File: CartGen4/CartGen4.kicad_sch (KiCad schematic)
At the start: 0 parts

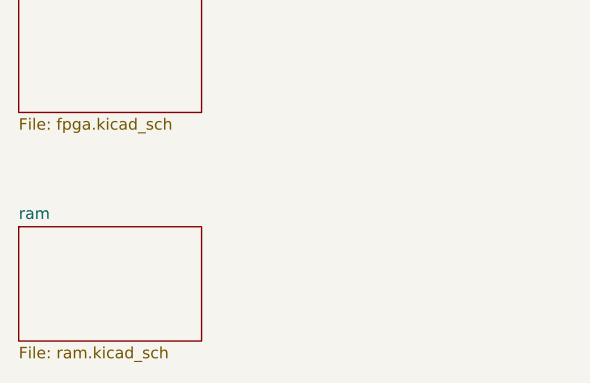
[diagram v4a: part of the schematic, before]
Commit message: Added SPI flash
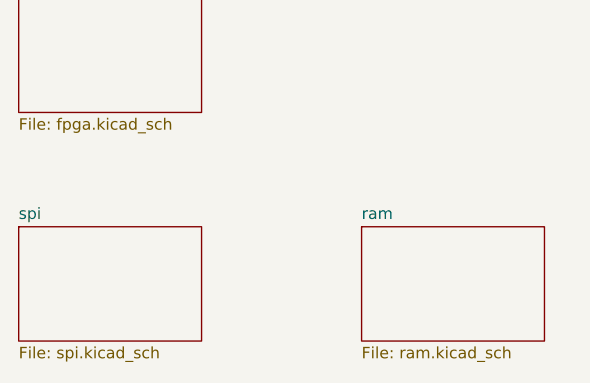
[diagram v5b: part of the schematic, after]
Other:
- added sheet spi (spi.kicad_sch)
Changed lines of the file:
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@@
     )
   )
-  (sheet (at 25.4 139.7) (size 20.32 12.7) (fields_autoplaced)
+  (sheet (at 63.5 139.7) (size 20.32 12.7) (fields_autoplaced)
     (stroke (width 0.1524) (type solid) (color 0 0 0 0))
     (fill (color 0 0 0 0.0000))
-    (property "Sheet name" "ram" (id 0) (at 25.4 138.9884 0)
+    (property "Sheet name" "ram" (id 0) (at 63.5 138.9884 0)
       (effects (font (size 1.27 1.27)) (justify left bottom))
     )
-    (property "Sheet file" "ram.kicad_sch" (id 1) (at 25.4 152.9846 0)
+    (property "Sheet file" "ram.kicad_sch" (id 1) (at 63.5 152.9846 0)
       (effects (font (size 1.27 1.27)) (justify left top))
     )
@@
     )
     (property "Sheet file" "fpga.kicad_sch" (id 1) (at 25.4 127.5846 0)
+      (effects (font (size 1.27 1.27)) (justify left top))
+    )
+  )
+  (sheet (at 25.4 139.7) (size 20.32 12.7) (fields_autoplaced)
+    (stroke (width 0.1524) (type solid) (color 0 0 0 0))
+    (fill (color 0 0 0 0.0000))
+    (property "Sheet name" "spi" (id 0) (at 25.4 138.9884 0)
+      (effects (font (size 1.27 1.27)) (justify left bottom))
+    )
+    (property "Sheet file" "spi.kicad_sch" (id 1) (at 25.4 152.9846 0)
       (effects (font (size 1.27 1.27)) (justify left top))
     )
@@
     (path "/89c162de-8374-4cb6-9c74-abac2a052a8d" (page "5"))
     (path "/6fc5aafb-5a22-4bda-8f08-f38eb0e112cc" (page "6"))
+    (path "/a842574a-62bd-4545-b3b1-b3137c6c2721" (page "7"))
   )
   (symbol_instances
@@
       (reference "#PWR049") (unit 1) (value "GND") (footprint "")
     )
+    (path "/a842574a-62bd-4545-b3b1-b3137c6c2721/01f7a23f-9fae-4580-836f-7911963d2c74"
+      (reference "#PWR?") (unit 1) (value "GND") (footprint "")
+    )
     (path "/67020394-371c-451d-9641-dd6c212cfc5e/139bed1b-d7ef-48f0-93a7-b2ee5c35ebdd"
       (reference "#PWR?") (unit 1) (value "+5V") (footprint "")
@@
       (reference "#PWR?") (unit 1) (value "GND") (footprint "")
     )
+    (path "/a842574a-62bd-4545-b3b1-b3137c6c2721/4694efdb-3b6d-491b-8dbf-ec3b4909295d"
+      (reference "#PWR?") (unit 1) (value "GND") (footprint "")
+    )
     (path "/67020394-371c-451d-9641-dd6c212cfc5e/4faf6052-5bf8-48ec-be57-0a6291be0b85"
       (reference "#PWR?") (unit 1) (value "+5V") (footprint "")
@@
       (reference "#PWR?") (unit 1) (value "+5V") (footprint "")
     )
-    (path "/76bc839d-93e8-4c60-b95d-ac552335ae99/a61a5a01-4844-4d68-865b-c6702144281d"
-      (reference "#PWR?") (unit 1) (value "GND") (footprint "")
-    )
-    (path "/76bc839d-93e8-4c60-b95d-ac552335ae99/b525956d-6c8a-4131-adb5-2cd5a66479ee"
-      (reference "#PWR?") (unit 1) (value "+3.3V") (footprint "")
+    (path "/a842574a-62bd-4545-b3b1-b3137c6c2721/97b2c2fb-5589-41f0-bcb4-c80098f1ce20"
+      (reference "#PWR?") (unit 1) (value "+3V3") (footprint "")
+    )
+    (path "/a842574a-62bd-4545-b3b1-b3137c6c2721/ae1dd4cd-b33f-493a-adda-4871546ee7b9"
+      (reference "#PWR?") (unit 1) (value "+3V3") (footprint "")
     )
     (path "/67020394-371c-451d-9641-dd6c212cfc5e/b9902037-5e38-4fae-b92f-82749be53d58"
       (reference "#PWR?") (unit 1) (value "+3.3V") (footprint "")
     )
-    (path "/76bc839d-93e8-4c60-b95d-ac552335ae99/c351d6bc-adb7-4d76-8e8b-e9cdf43a3fa6"
-      (reference "#PWR?") (unit 1) (value "GND") (footprint "")
+    (path "/a842574a-62bd-4545-b3b1-b3137c6c2721/b9c089e3-6a98-47b3-879b-4d798bdf2bda"
+      (reference "#PWR?") (unit 1) (value "+3.3V") (footprint "")
     )
     (path "/67020394-371c-451d-9641-dd6c212cfc5e/c8f893a1-4dd0-448d-a737-07fa90198d44"
@@
       (reference "#PWR?") (unit 1) (value "GND") (footprint "")
     )
+    (path "/a842574a-62bd-4545-b3b1-b3137c6c2721/d689d778-0523-4cbc-9466-6e6a20f00bb2"
+      (reference "#PWR?") (unit 1) (value "GND") (footprint "")
+    )
     (path "/76bc839d-93e8-4c60-b95d-ac552335ae99/da54cb89-4c60-42cf-966f-c05231fcc60a"
       (reference "#PWR?") (unit 1) (value "GND") (footprint "")
@@
       (reference "#PWR?") (unit 1) (value "+1V8") (footprint "")
     )
+    (path "/a842574a-62bd-4545-b3b1-b3137c6c2721/ed1165e3-7705-4873-b53f-6932253f6de3"
+      (reference "#PWR?") (unit 1) (value "GND") (footprint "")
+    )
     (path "/4ef07d45-f940-4cb6-bb96-2ddec13fd099/1b8d5810-67b5-41f5-a4e9-e6c2cc9fec50"
       (reference "A1") (unit 1) (value "GBC_Cart") (footprint "Boards:GBC_Cart")
@@
       (reference "C29") (unit 1) (value "100n") (footprint "")
     )
-    (path "/76bc839d-93e8-4c60-b95d-ac552335ae99/4dc2785f-70ea-455a-a576-3c552ffd6bf7"
+    (path "/a842574a-62bd-4545-b3b1-b3137c6c2721/373bb0b0-a4d2-4f2a-8738-01c5270f27b1"
+      (reference "C?") (unit 1) (value "100n") (footprint "")
+    )
+    (path "/a842574a-62bd-4545-b3b1-b3137c6c2721/98a36b99-198d-4837-aeab-8049fd52403d"
       (reference "C?") (unit 1) (value "100n") (footprint "")
     )
@@
       (reference "R?") (unit 1) (value "50K") (footprint "")
     )
+    (path "/a842574a-62bd-4545-b3b1-b3137c6c2721/f0f02253-49b5-4d4f-af3f-1b2d3b690b4e"
+      (reference "R?") (unit 1) (value "15K") (footprint "")
+    )
     (path "/4ef07d45-f940-4cb6-bb96-2ddec13fd099/e190d083-d82d-481a-a7b8-1c8c0afec670"
       (reference "U1") (unit 1) (value "TPS65266-1RHBR") (footprint "QFN50P500X500X100-33N-D")
@@
       (reference "U?") (unit 1) (value "LSF0204GU12X") (footprint "")
     )
-    (path "/76bc839d-93e8-4c60-b95d-ac552335ae99/89742353-c7fb-4a5c-92c0-bd1a58893870"
-      (reference "U?") (unit 1) (value "DS1391U-33+") (footprint "")
-    )
     (path "/67020394-371c-451d-9641-dd6c212cfc5e/9e11e768-52c8-4cf8-8274-a0ba02779823"
       (reference "U?") (unit 1) (value "NXS0108BQX") (footprint "")
@@
       (reference "U?") (unit 1) (value "SIT8008BI-73-33E-33.333333G") (footprint "")
     )
+    (path "/a842574a-62bd-4545-b3b1-b3137c6c2721/b7d7d485-eae8-414c-ac57-f0b0d0b494e9"
+      (reference "U?") (unit 1) (value "IS25WP080D-JNLE") (footprint "")
+    )
+    (path "/a842574a-62bd-4545-b3b1-b3137c6c2721/e6de6545-d930-4c64-ad23-677586f8f563"
+      (reference "U?") (unit 1) (value "DS1391U-33+") (footprint "")
+    )
     (path "/89c162de-8374-4cb6-9c74-abac2a052a8d/1765047d-477d-4e9e-a14b-c311772de8ac"
       (reference "U?") (unit 2) (value "LFXP2-8E-5MN132C") (footprint "")
@@
       (reference "U?") (unit 10) (value "LFXP2-8E-5MN132C") (footprint "")
     )
-    (path "/76bc839d-93e8-4c60-b95d-ac552335ae99/a9f9e9c7-ee28-4e48-9d3e-51aeed2f5c79"
+    (path "/a842574a-62bd-4545-b3b1-b3137c6c2721/7407e75c-0b18-4925-ae3b-8416f140b724"
       (reference "Y?") (unit 1) (value "FC-135R_32.7680KA-E5") (footprint "")
     )
